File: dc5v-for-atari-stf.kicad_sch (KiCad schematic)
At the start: 4 parts

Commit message: do the schematic
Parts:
- added D?: LED, symbol Device:LED
- added J?: Conn_01x02, symbol Connector_Generic:Conn_01x02
- added R?: 2K, symbol Device:R_Small_US
- added SW?: Momentary or Latched, symbol Switch:SW_Push
- J?: value Conn_01x04 -> Adjustable MT3608 module
- J?: value Conn_01x04 -> Fixed 12V module
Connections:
- net +12V: now reaches J?.1 (Pin_1)
- net +12V: now also J?.1 (Pin_1), J?.6 (Pin_6)
- net GND: now reaches J?.2 (Pin_2)
- net GND: now also J?.2 (Pin_2), J?.2 (Pin_2), J?.3 (Pin_3), J?.3 (Pin_3), J?.3 (Pin_3), J?.4 (Pin_4), J?.5 (Pin_5), D?.1 (K), J?.2 (Pin_2)
- net +5V: now reaches J?.4 (Pin_4)
- net +5V: now also J?.1 (Pin_1), J?.1 (Pin_1), J?.2 (Pin_2), J?.4 (Pin_4), J?.1 (Pin_1), SW?.1
- new net: R?.1, SW?.2
- new net: D?.2 (A), R?.2
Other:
- note added: "Adjustable MT3608 Module : https://www.az-delivery.de/fr/products/mt3608-dc-dc-step-up-modul-1 A 17.4×37 mm module, with one pin on each corner, and a trimpot to adjust the output voltage. MUST be adjusted to output 12V."
- note added: "BEFORE plugging anything else (dc-dc 12V converter, mainboard, ...), one MUST check that the wiring to the rocker switch is correct by using the LED."
- note added: "Connection to another device (2-3W max)"
- note added: "Connection to rocker switch"
- note added: "DC-DC 12V step-up modules"
- note added: "Fixed 12V module : https://www.exxosforum.co.uk/atari/store2/#0223 https://fr.aliexpress.com/item/1005005916306503.html A small (10.16×20.5 mm) module with a row of 4 pins, with a 2.54 mm pitch, that outputs 12V. With a 5V input, the max current is stated at 370 mA. The pins MUST be reinstalled to be on the backside instead of the component side."
- note added: "Main connection to main board"
- moved on the sheet: J?

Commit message: metadata of the schematic
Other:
- company: (none) -> Sporniket
- title: (none) -> DC5V for the Atari STF
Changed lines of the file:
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@@
   (paper "A4" portrait)
   (title_block
+    (title "DC5V for the Atari STF")
     (date "2023-08-22")
+    (rev "v1.0.0-DRAFT")
+    (company "Sporniket")
+    (comment 4 "https://github.com/sporniket/dc5v-for-atari-stf")
   )
   (junction (at 165.1 53.34) (diameter 0) (color 0 0 0 0)

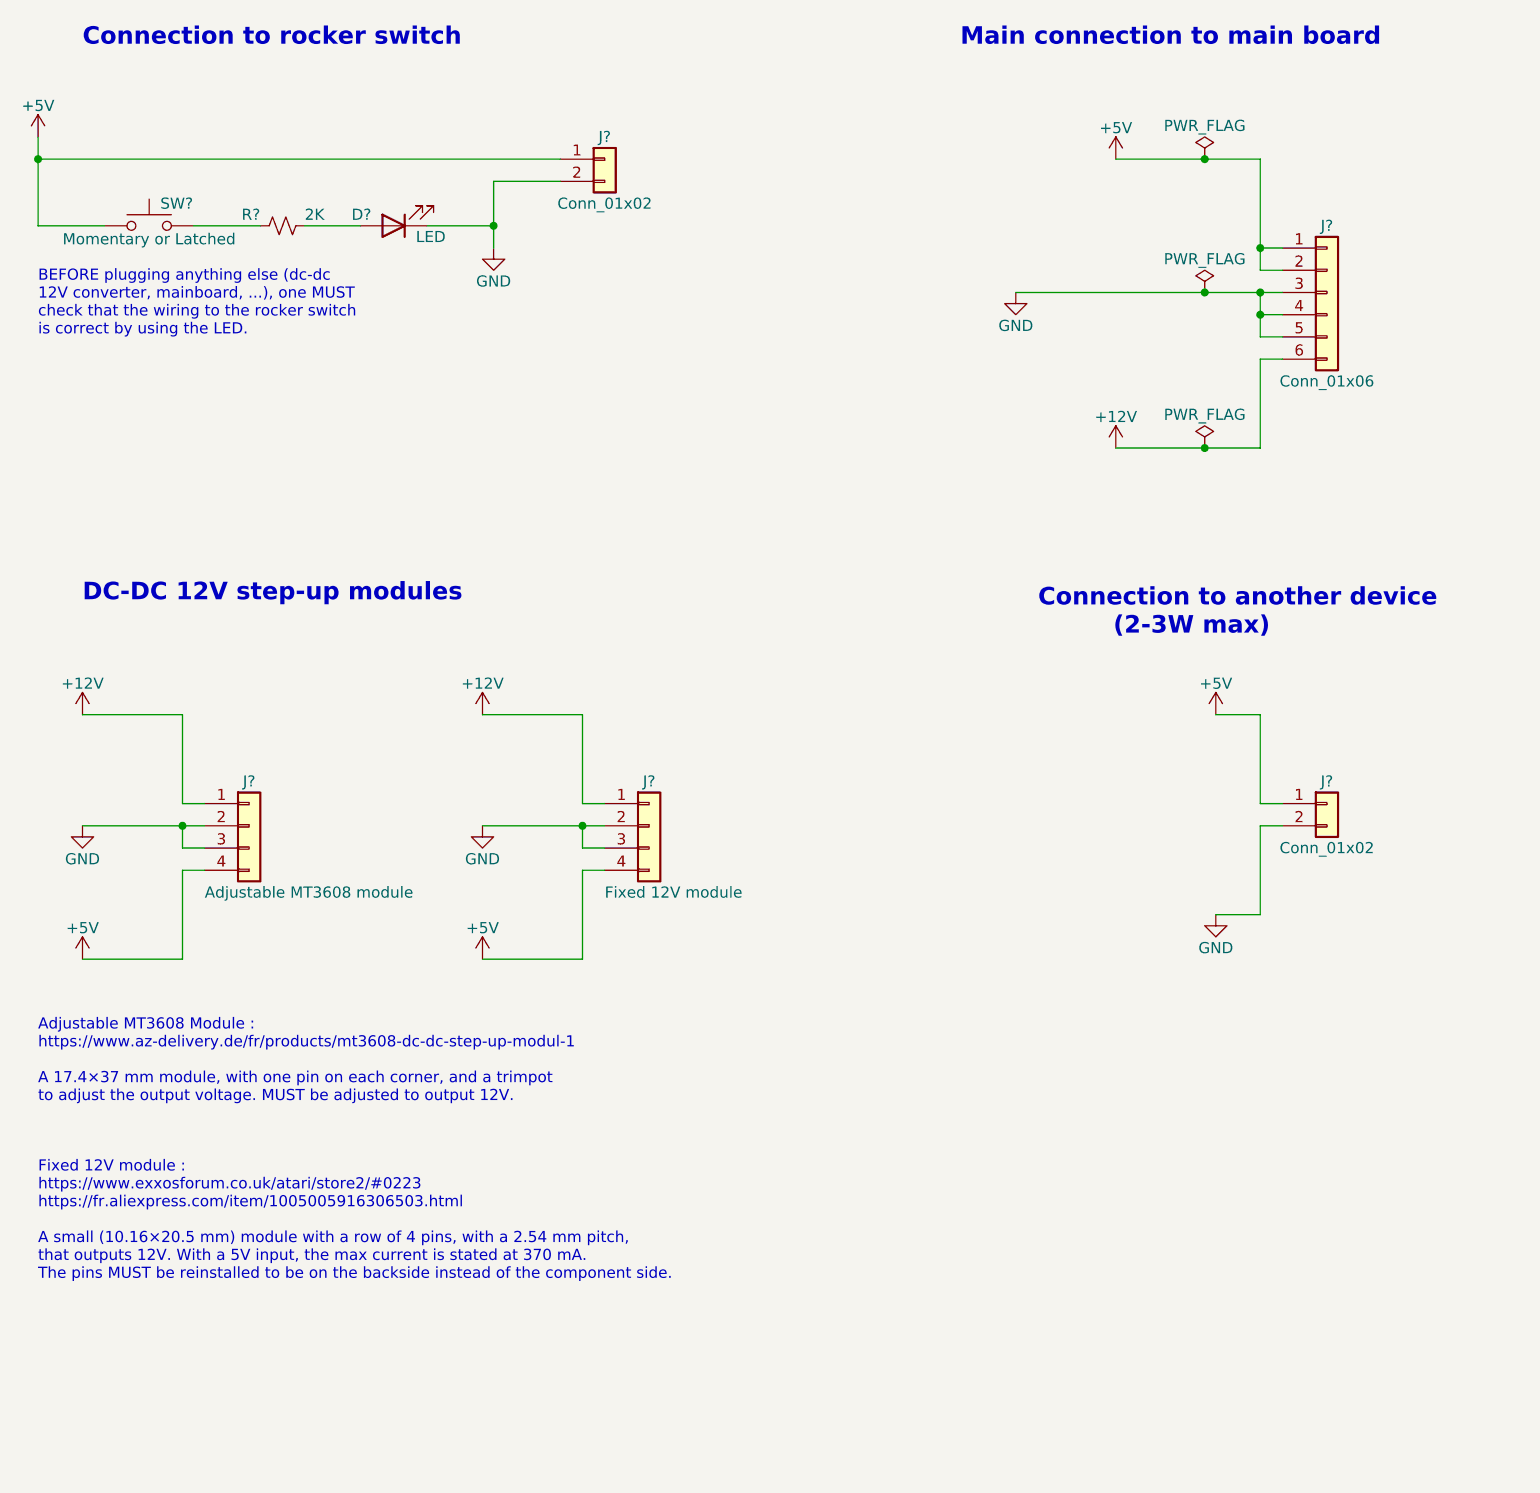
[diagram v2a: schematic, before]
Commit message: Numbers on symbols, add footprint so that SW1 can be either push button or latched push-push button
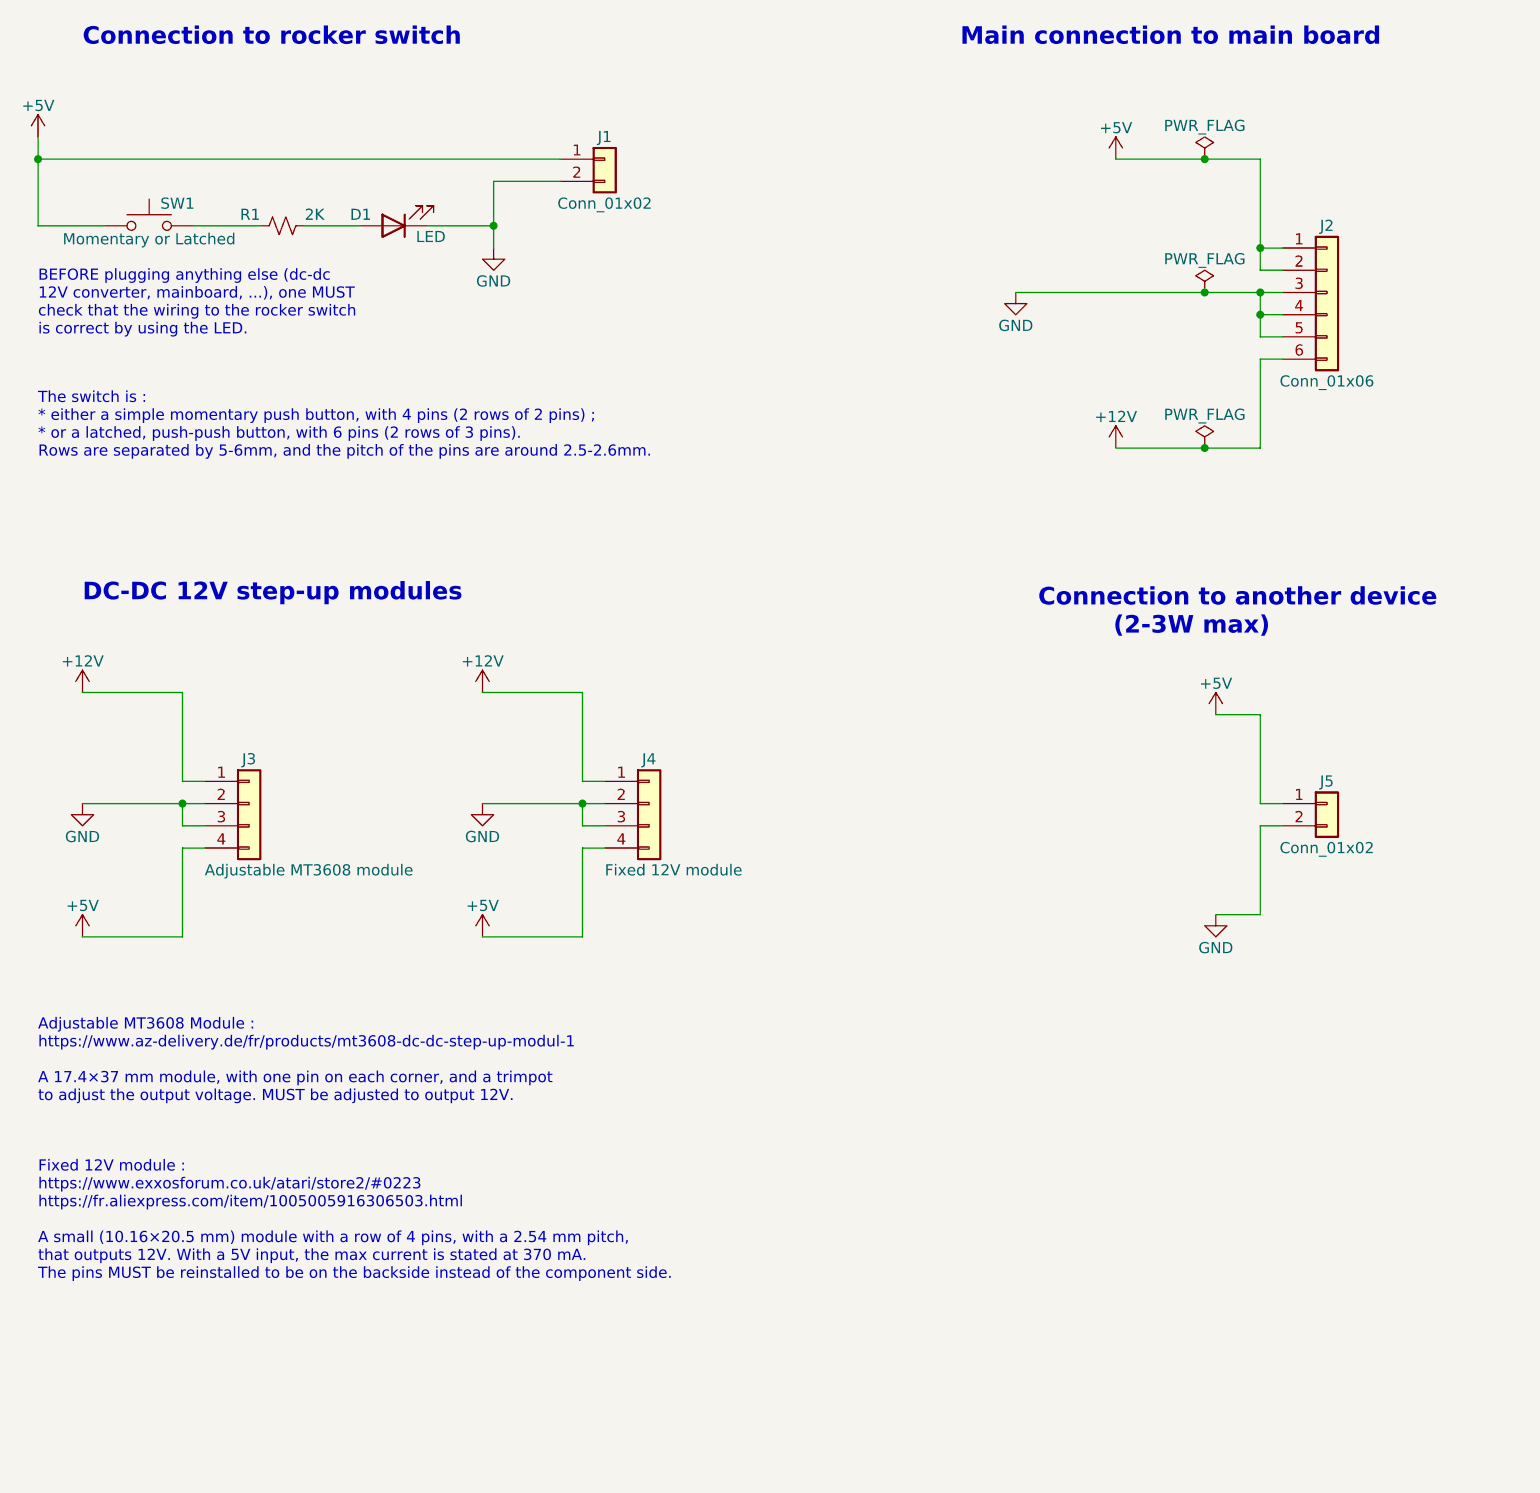
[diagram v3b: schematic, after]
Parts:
- gave numbers to parts that had none: 8
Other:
- note added: "The switch is : * either a simple momentary push button, with 4 pins (2 rows of 2 pins) ; * or a latched, push-push button, with 6 pins (2 rows of 3 pins). Rows are separated by 5-6mm, and the pitch of the pins are around 2.5-2.6mm."
- moved on the sheet: J3, J4
